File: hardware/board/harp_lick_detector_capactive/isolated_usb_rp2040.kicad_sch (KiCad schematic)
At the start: 49 parts, among them J2 Conn_01x03_Male, J4 AudioJack3, J5 USB_C_Receptacle_USB2.0, U2 TPD2EUSB30, U3 ADUM4160, U4 RP2040, U5 W25Q16JVUXIQ, X1 ECS-TXO-2016

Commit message: update lickety split 0.6.1 pcb files
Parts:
- J4: Alternate SJ-3523-SMT-TR -> (none); Link https://www.digikey.com/en/products/detail/cui-devices/SJ-3524-SMT-TR-BE/2295987 -> https://www.digikey.com/en/products/detail/cui-devices/SJ-3523-SMT-TR/281297; Manufacturer Number SJ-3524-SMT-TR-BE -> SJ-3523-SMT-TR
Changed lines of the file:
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@@
       (effects (font (size 1.27 1.27)) hide)
     )
-    (property "Link" "https://www.digikey.com/en/products/detail/cui-devices/SJ-3524-SMT-TR-BE/2295987" (at 24.13 121.285 0)
+    (property "Link" "https://www.digikey.com/en/products/detail/cui-devices/SJ-3523-SMT-TR/281297" (at 24.13 121.285 0)
       (effects (font (size 1.27 1.27)) hide)
     )
@@
       (effects (font (size 1.27 1.27)) hide)
     )
-    (property "Manufacturer Number" "SJ-3524-SMT-TR-BE" (at 24.13 121.285 0)
+    (property "Manufacturer Number" "SJ-3523-SMT-TR" (at 24.13 121.285 0)
       (effects (font (size 1.27 1.27)) hide)
     )
-    (property "Alternate" "SJ-3523-SMT-TR" (at 24.13 121.285 0)
-      (effects (font (size 1.27 1.27)) hide)
-    )

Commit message: draft v0.7 pcb schematic and layout
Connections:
- net FILTER_SEL: now reaches U4.27 (GPIO16)
- net GAIN_SEL: now reaches U4.28 (GPIO17)
- net 125KHZ_OUT: now reaches U4.5 (GPIO3)
- net 100KHZ_SQ_WAVE_OUT renamed 100KHZ_OUT
- no-connect marks 28 -> 25
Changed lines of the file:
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@@
   (no_connect (at 245.11 89.535))
   (no_connect (at 245.11 94.615))
-  (no_connect (at 245.11 114.935))
   (no_connect (at 245.11 109.855))
   (no_connect (at 245.11 112.395))
@@
   (no_connect (at 245.11 104.775))
   (no_connect (at 245.11 84.455))
-  (no_connect (at 245.11 81.915))
   (no_connect (at 245.11 97.155))
   (no_connect (at 43.18 52.705))
   (no_connect (at 181.61 139.065))
-  (no_connect (at 245.11 117.475))
   (no_connect (at 245.11 99.695))
   (no_connect (at 181.61 141.605))
@@
     (stroke (width 0) (type default))
   )
+  (wire (pts (xy 245.11 114.935) (xy 255.27 114.935))
+    (stroke (width 0) (type default))
+  )
   (wire (pts (xy 125.73 180.975) (xy 125.73 179.705))
     (stroke (width 0) (type default))
@@
     (stroke (width 0) (type default))
   )
+  (wire (pts (xy 245.11 81.915) (xy 247.65 81.915))
+    (stroke (width 0) (type default))
+  )
   (wire (pts (xy 255.27 135.255) (xy 255.27 133.35))
     (stroke (width 0) (type default))
@@
     (stroke (width 0) (type default))
   )
+  (wire (pts (xy 245.11 117.475) (xy 255.27 117.475))
+    (stroke (width 0) (type default))
+  )
   (wire (pts (xy 45.72 43.815) (xy 70.485 43.815))
     (stroke (width 0) (type default))
@@
     (effects (font (size 1.27 1.27)) (justify left bottom))
   )
+  (global_label "GAIN_SEL" (shape input) (at 255.27 117.475 0) (fields_autoplaced)
+    (effects (font (size 1.27 1.27)) (justify left))
+    (property "Intersheetrefs" "${INTERSHEET_REFS}" (at 266.9033 117.475 0)
+      (effects (font (size 1.27 1.27)) (justify left) hide)
+    )
+  )
+  (global_label "FILTER_SEL" (shape input) (at 255.27 114.935 0) (fields_autoplaced)
+    (effects (font (size 1.27 1.27)) (justify left))
+    (property "Intersheetrefs" "${INTERSHEET_REFS}" (at 268.7175 114.935 0)
+      (effects (font (size 1.27 1.27)) (justify left) hide)
+    )
+  )
   (hierarchical_label "PIO_SCK" (shape input) (at 255.27 125.095 0) (fields_autoplaced)
     (effects (font (size 1.27 1.27)) (justify left))
   )
-  (hierarchical_label "100KHZ_SQ_WAVE_OUT" (shape input) (at 247.65 79.375 0) (fields_autoplaced)
+  (hierarchical_label "100KHZ_OUT" (shape input) (at 247.65 79.375 0) (fields_autoplaced)
+    (effects (font (size 1.27 1.27)) (justify left))
+  )
+  (hierarchical_label "125KHZ_OUT" (shape input) (at 247.65 81.915 0) (fields_autoplaced)
     (effects (font (size 1.27 1.27)) (justify left))
   )

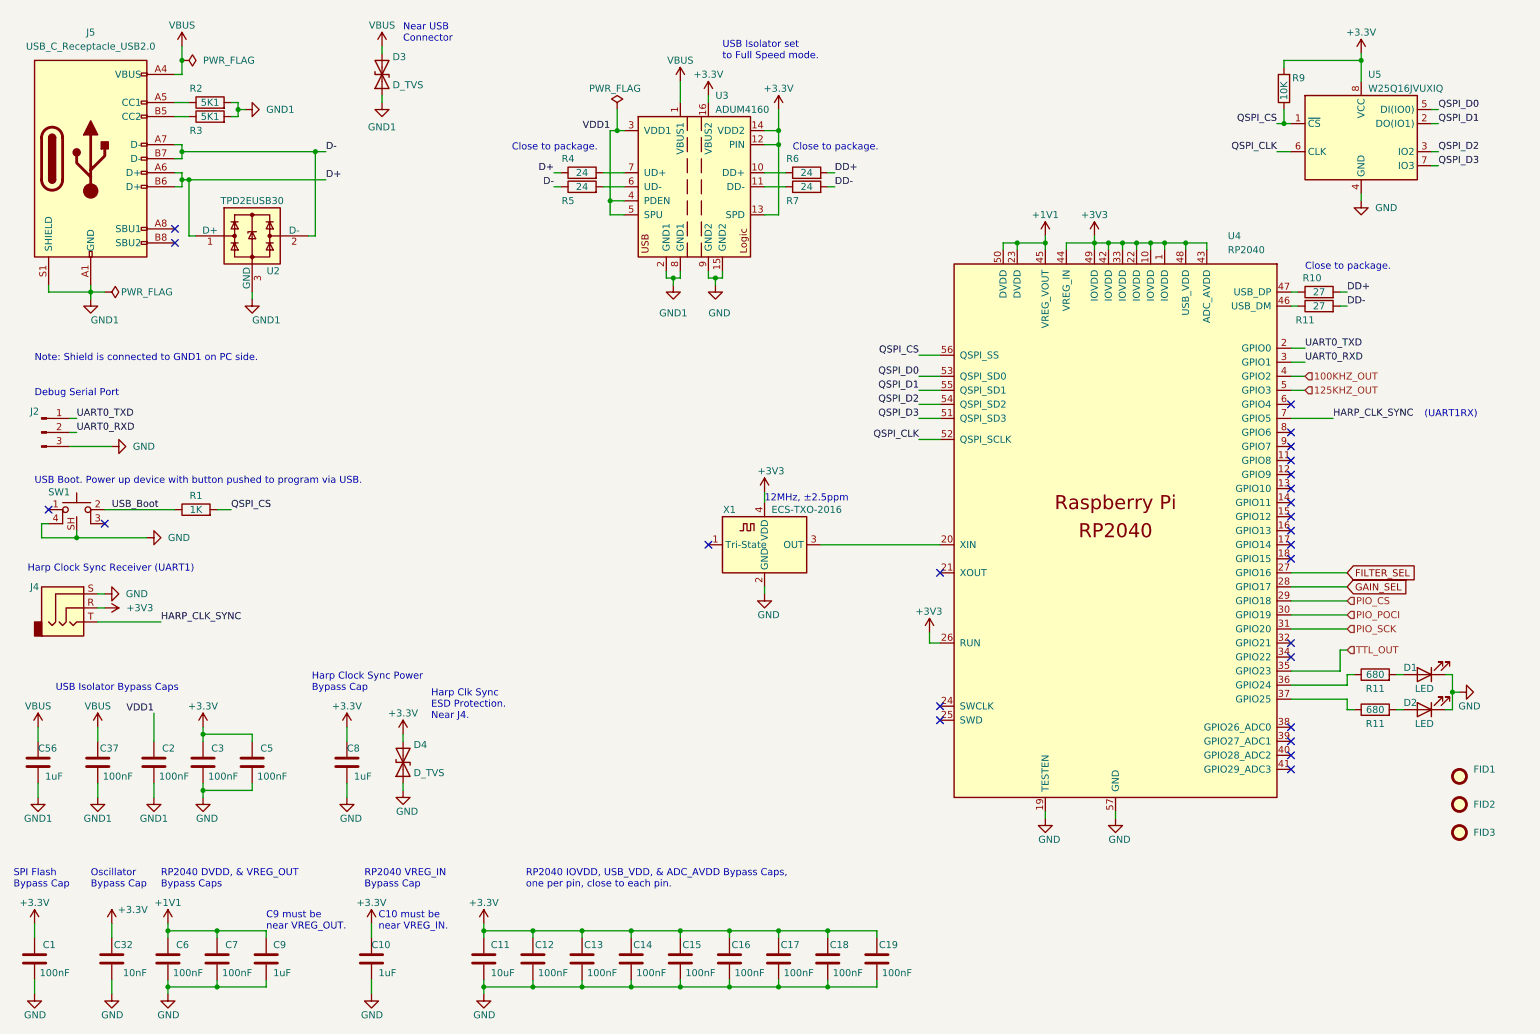
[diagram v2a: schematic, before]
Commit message: implement soe feedback in layout
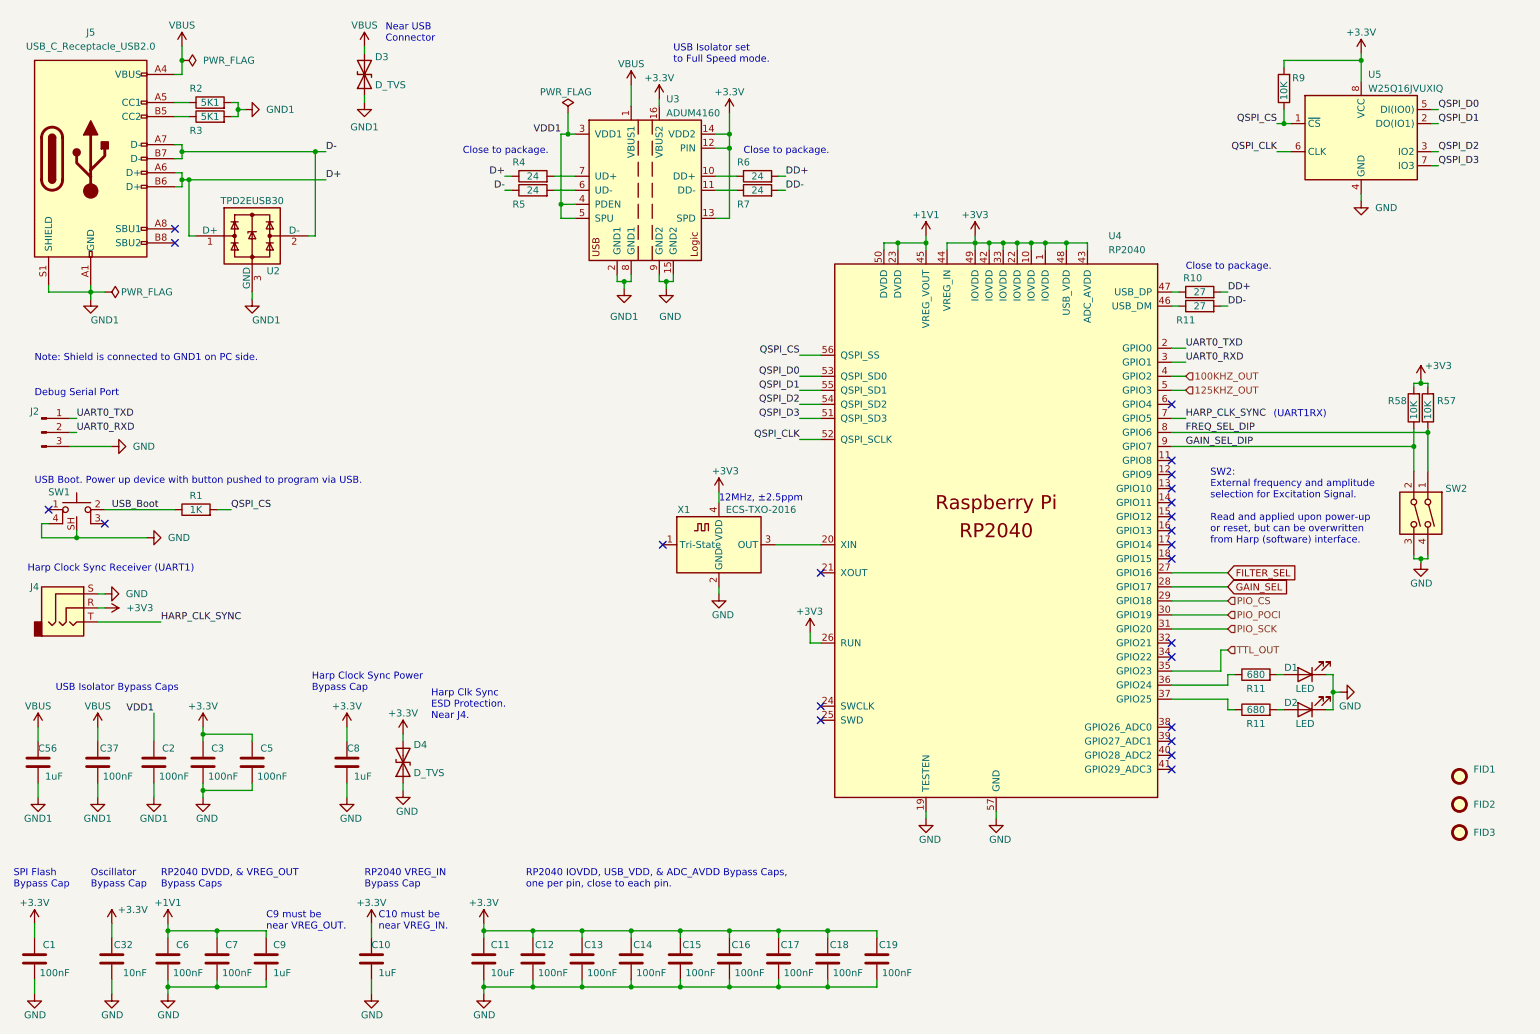
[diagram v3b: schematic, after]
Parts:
- added R57, R58: 10K, Resistor_SMD:R_0402_1005Metric, symbol Device:R
- added SW2: SW_DIP_x02, Button_Switch_SMD:SW_DIP_SPSTx02_Slide_9.78x7.26mm_W8.61mm_P2.54mm, symbol Switch:SW_DIP_x02
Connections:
- net +3V3: now also R57.2, R58.2
- net GND: now also SW2.3, SW2.4
- net FREQ_SEL_DIP: now reaches U4.8 (GPIO6)
- net FREQ_SEL_DIP: now also R57.1, SW2.1
- net GAIN_SEL_DIP: now reaches U4.9 (GPIO7)
- net GAIN_SEL_DIP: now also R58.1, SW2.2
- no-connect marks 25 -> 23
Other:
- note added: "SW2: External frequency and amplitude selection for Excitation Signal. Read and applied upon power-up or reset, but can be overwritten from Harp (software) interface."
- moved on the sheet: D1, D2, D3, R10, R11, R4, R5, R6, R7, U3, U4, X1

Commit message: draft v0.8 pcb layout
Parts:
- added R19 (x2): 1K00, Resistor_SMD:R_0402_1005Metric, symbol Device:R
- added R8 (x2): 4K7, Resistor_SMD:R_0402_1005Metric, symbol Device:R
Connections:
- net GAIN_SEL: now also R19.2
- net GND: now also R8.2, R8.2
- net +3V3 renamed +3.3V
- net FILTER_SEL renamed FREQ_SEL
- net FREQ_SEL: now also R19.2
- new net FREQ_SEL_2V5: R19.1, R8.1
- new net GAIN_SEL_2V5: R19.1, R8.1
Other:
- note added: "Divide down 3.3V outputs to be less than (2.5 + 0.3)V for MAX4564."
- moved on the sheet: D1, D2, D3, FID1, FID2, FID3, J5, R10, R11, R2, R3, R4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

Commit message: update board with filter resistor values
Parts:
- J4: footprint Connector_Audio:Jack_3.5mm_CUI_SJ-3523-SMT_Horizontal -> Connector_Audio:Jack_3.5mm_CUI_SJ-3524-SMT_Horizontal; Link https://www.digikey.com/en/products/detail/cui-devices/SJ-3523-SMT-TR/281297 -> https://www.digikey.com/en/products/detail/cui-devices/SJ-3524-SMT-TR-BE/2295987; Manufacturer Number SJ-3523-SMT-TR -> SJ-3524-SMT-TR-BE; PCBWay Link https://www.pcbway.com/components/detail/SJ3523SMTTR/473228/ -> (none)
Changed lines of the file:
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@@
       (effects (font (size 1.27 1.27)) hide)
     )
-    (property "Footprint" "Connector_Audio:Jack_3.5mm_CUI_SJ-3523-SMT_Horizontal" (at 24.13 121.285 0)
+    (property "Footprint" "Connector_Audio:Jack_3.5mm_CUI_SJ-3524-SMT_Horizontal" (at 24.13 121.285 0)
       (effects (font (size 1.27 1.27)) hide)
     )
@@
       (effects (font (size 1.27 1.27)) hide)
     )
-    (property "Link" "https://www.digikey.com/en/products/detail/cui-devices/SJ-3523-SMT-TR/281297" (at 24.13 121.285 0)
+    (property "Link" "https://www.digikey.com/en/products/detail/cui-devices/SJ-3524-SMT-TR-BE/2295987" (at 24.13 121.285 0)
       (effects (font (size 1.27 1.27)) hide)
     )
-    (property "PCBWay Link" "https://www.pcbway.com/components/detail/SJ3523SMTTR/473228/" (at 24.13 121.285 0)
+    (property "Manufacturer Number" "SJ-3524-SMT-TR-BE" (at 24.13 121.285 0)
       (effects (font (size 1.27 1.27)) hide)
     )
-    (property "Manufacturer Number" "SJ-3523-SMT-TR" (at 24.13 121.285 0)
-      (effects (font (size 1.27 1.27)) hide)
-    )

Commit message: finish rev8
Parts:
- D3, D4: Link https://www.digikey.com/en/products/detail/onsemi/SZESDM355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 -> https://www.digikey.com/en/products/detail/onsemi/ESD7571N2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; Manufacturer Number SZESDM3551N2T5G -> ESD7571N2T5G; PCBWay Link https://www.pcbway.com/components/detail/SZESDM3551N2T5G/94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 -> (none)
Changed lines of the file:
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@@
       (effects (font (size 1.27 1.27)) hide)
     )
-    (property "Datasheet" "https://www.onsemi.com/pdf/datasheet/esdm3551-d.pdf" (at 84.455 149.225 0)
-      (effects (font (size 1.27 1.27)) hide)
-    )
-    (property "Link" "https://www.digikey.com/en/products/detail/onsemi/SZESDM3551N2T5G/15860141" (at 84.455 149.225 0)
-      (effects (font (size 1.27 1.27)) hide)
-    )
-    (property "PCBWay Link" "https://www.pcbway.com/components/detail/SZESDM3551N2T5G/947288/" (at 84.455 149.225 0)
+    (property "Datasheet" "https://www.onsemi.com/pdf/datasheet/esd7571-d.pdf" (at 84.455 149.225 0)
+      (effects (font (size 1.27 1.27)) hide)
+    )
+    (property "Link" "https://www.digikey.com/en/products/detail/onsemi/ESD7571N2T5G/7220690" (at 84.455 149.225 0)
       (effects (font (size 1.27 1.27)) hide)
     )
@@
       (effects (font (size 1.27 1.27)) hide)
     )
-    (property "Manufacturer Number" "SZESDM3551N2T5G" (at 84.455 149.225 0)
+    (property "Manufacturer Number" "ESD7571N2T5G" (at 84.455 149.225 0)
       (effects (font (size 1.27 1.27)) hide)
     )
@@
       (effects (font (size 1.27 1.27)) hide)
     )
-    (property "Datasheet" "https://www.onsemi.com/pdf/datasheet/esdm3551-d.pdf" (at 70.485 23.495 0)
-      (effects (font (size 1.27 1.27)) hide)
-    )
-    (property "Link" "https://www.digikey.com/en/products/detail/onsemi/SZESDM3551N2T5G/15860141" (at 70.485 23.495 0)
-      (effects (font (size 1.27 1.27)) hide)
-    )
-    (property "PCBWay Link" "https://www.pcbway.com/components/detail/SZESDM3551N2T5G/947288/" (at 70.485 23.495 0)
+    (property "Datasheet" "https://www.onsemi.com/pdf/datasheet/esd7571-d.pdf" (at 70.485 23.495 0)
+      (effects (font (size 1.27 1.27)) hide)
+    )
+    (property "Link" "https://www.digikey.com/en/products/detail/onsemi/ESD7571N2T5G/7220690" (at 70.485 23.495 0)
       (effects (font (size 1.27 1.27)) hide)
     )
@@
       (effects (font (size 1.27 1.27)) hide)
     )
-    (property "Manufacturer Number" "SZESDM3551N2T5G" (at 70.485 23.495 0)
-      (effects (font (size 1.27 1.27)) hide)
-    )
+    (property "Manufacturer Number" "ESD7571N2T5G" (at 70.485 23.495 0)
+      (effects (font (size 1.27 1.27)) hide)
+    )

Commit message: update to new harp core
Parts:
- renumbered C32 to C4, R8 to R60, R8 to R61, R19 to R74, R19 to R75
